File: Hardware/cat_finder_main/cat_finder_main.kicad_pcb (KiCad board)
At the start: 2 copper layers, 85 x 70 mm, 38 parts, among them J1 BATT, J10 Analog, J2 BME280, J3 CSS811, J4 DRIVERS, J5 GY-87, J7 FTDI, J8 Digital, U1 LD1117A33, U2 MCP732831CHARGER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

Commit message: clone other repo
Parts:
- renumbered SDA to J6, I2C to J9
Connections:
- J3 pad 5: /WAKE -> GND
- J3 pad 6: /INTCSS -> +3V3
- J3 pad 7: /RESET -> +3V3
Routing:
- net +3V3: track 170.8 -> 177.9 mm

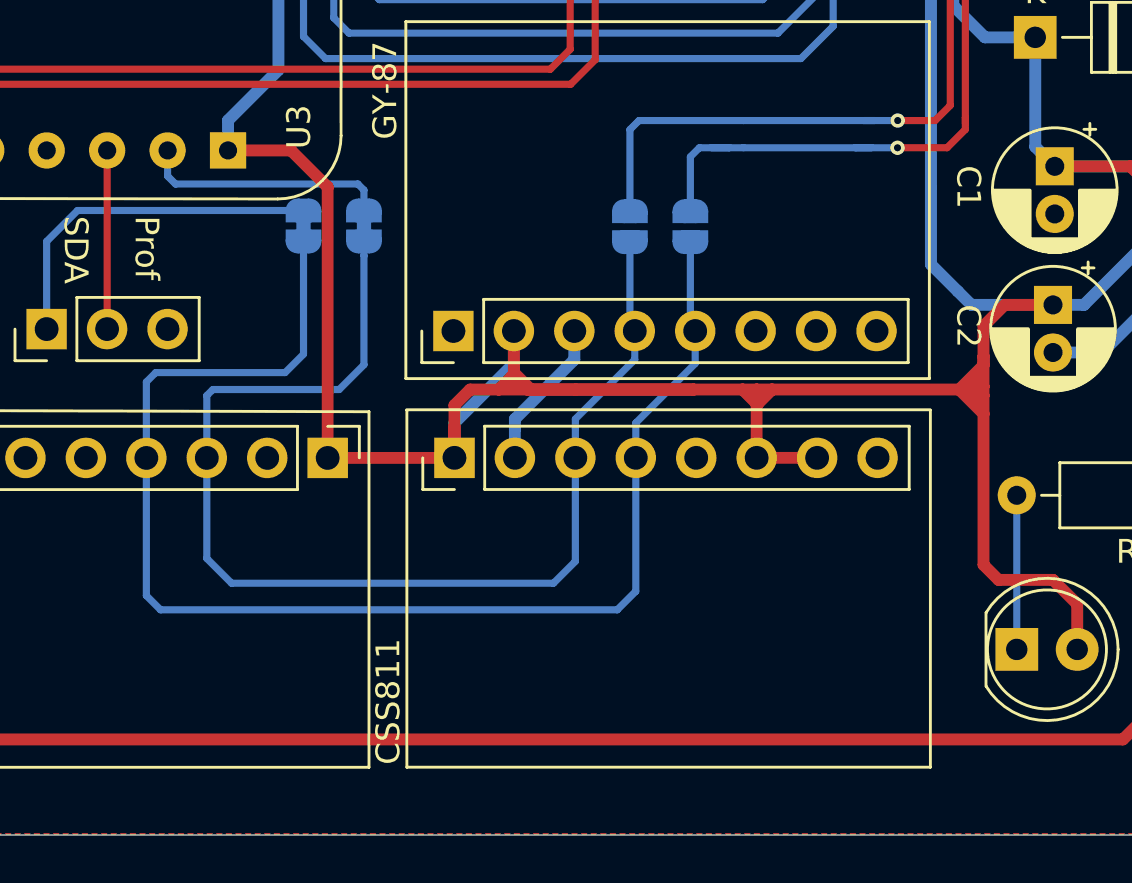
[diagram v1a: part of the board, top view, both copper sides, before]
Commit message: change CCS811
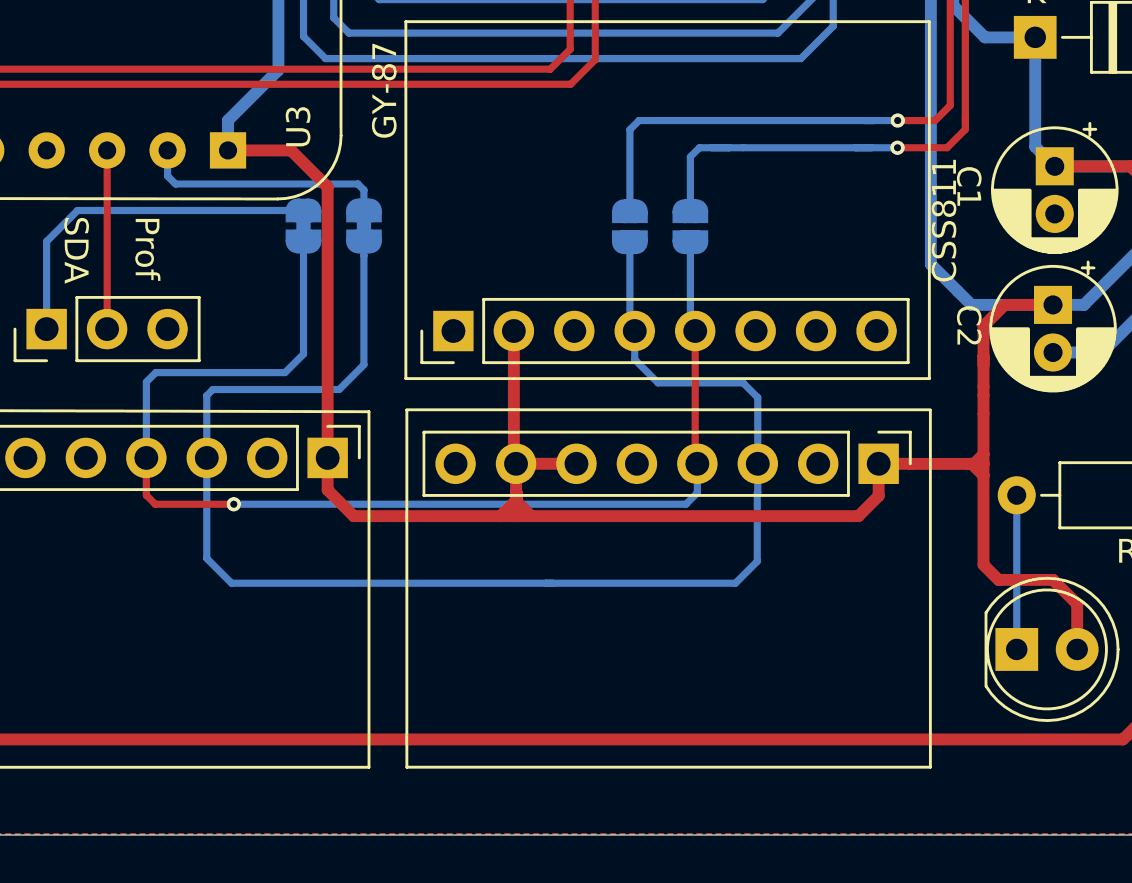
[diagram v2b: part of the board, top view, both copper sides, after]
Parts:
- moved J3 17.8 mm to (162.6, 114.5), turned to 270 degrees
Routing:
- net +3V3: track 177.9 -> 162.6 mm
- net /SCL: track 49.8 -> 60.9 mm
- net /SDA: track 57.5 -> 50.5 mm, vias 0 -> 1
- net GND: track 23.3 -> 16.9 mm

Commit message: labels battery
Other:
- board text added: "5V IN"
- board text added: "Battery Out"
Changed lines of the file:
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@@
   (general
     (thickness 1.6)
-    (drawings 6386)
+    (drawings 6388)
     (tracks 304)
     (zones 0)
@@
   (page A4)
   (layers
-    (0 F.Cu signal)
-    (31 B.Cu signal)
+    (0 F.Cu signal hide)
+    (31 B.Cu signal hide)
     (32 B.Adhes user)
     (33 F.Adhes user)
@@
     )
   )
+  (gr_text "Battery Out" (at 179.8 87 90) (layer F.SilkS)
+    (effects (font (size 1 1) (thickness 0.15)))
+  )
+  (gr_text "5V IN" (at 168.2 86.9 270) (layer F.SilkS)
+    (effects (font (size 1 1) (thickness 0.15)))
+  )
   (gr_line (start 119.38 119.38) (end 165.1 119.38) (layer B.SilkS) (width 0.12))

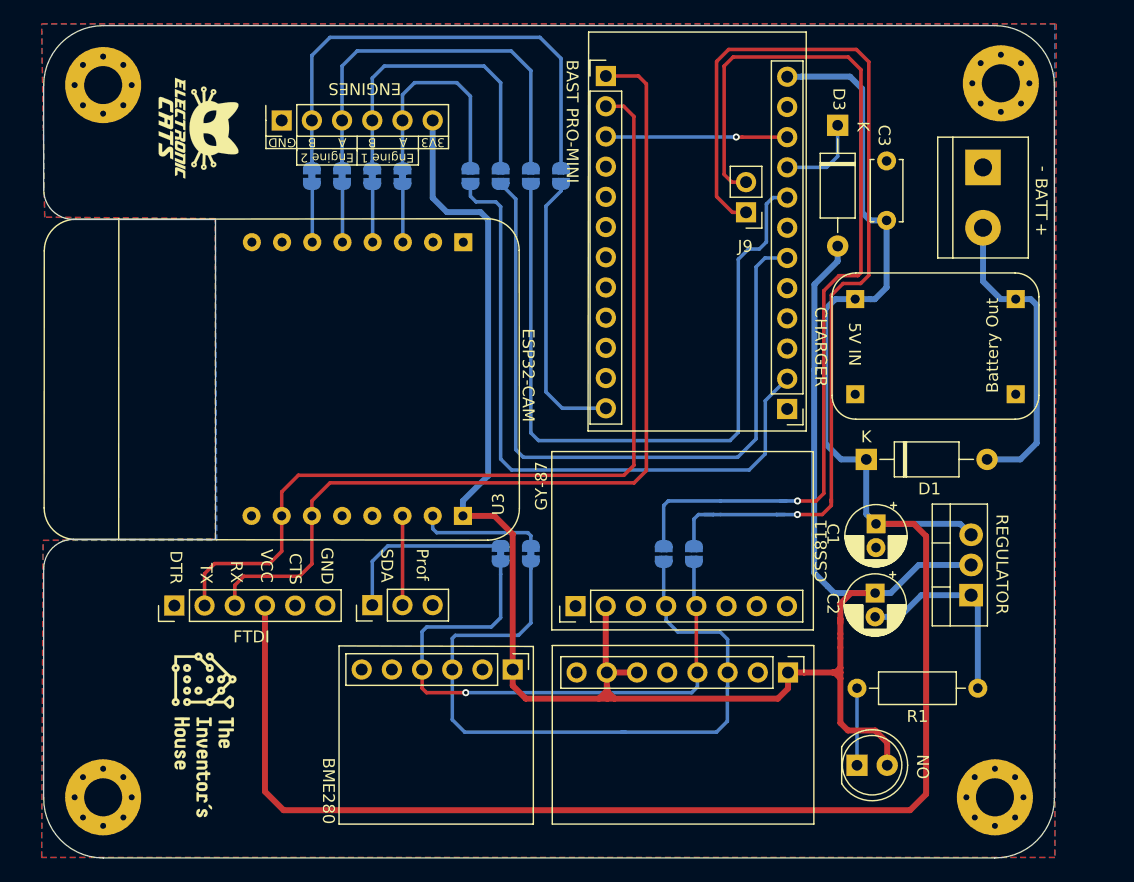
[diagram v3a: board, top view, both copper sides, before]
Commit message: change drill esp32
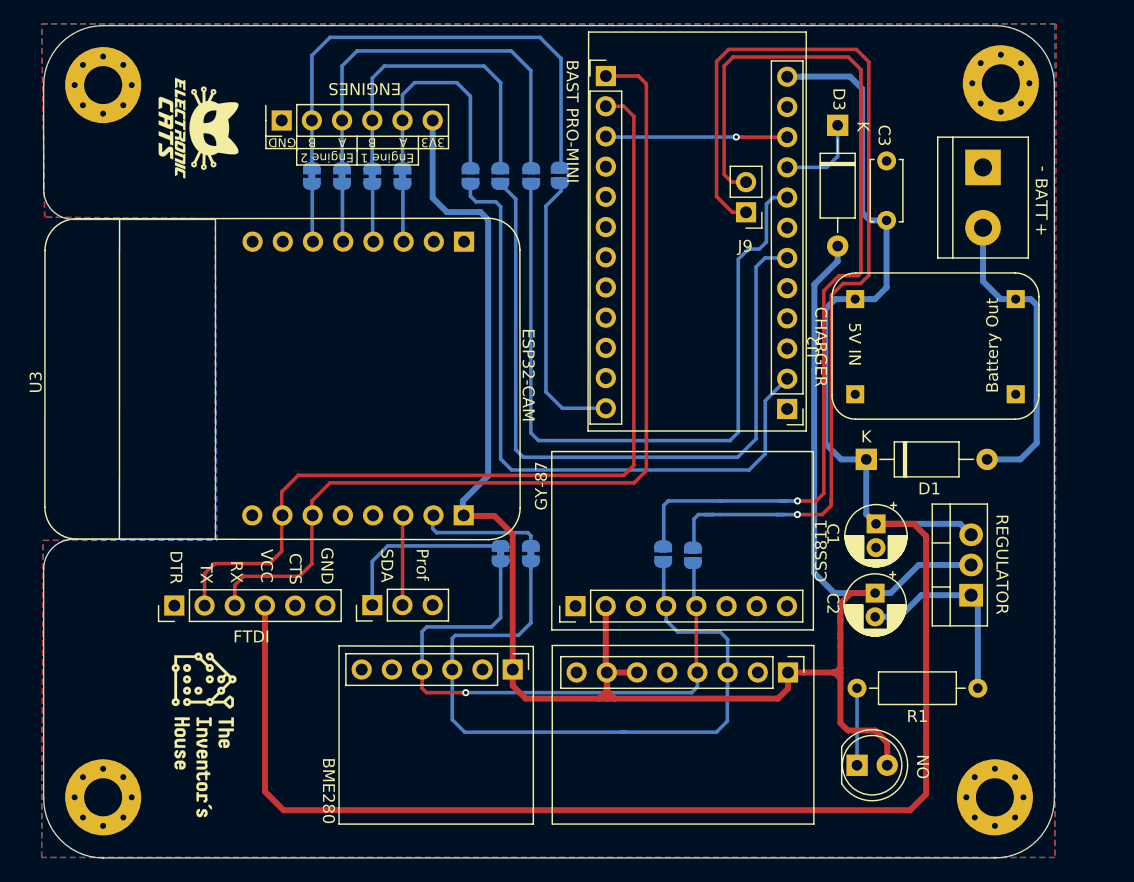
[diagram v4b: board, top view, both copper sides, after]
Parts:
- JP7: value Engine 1A -> Engine 1 A
- moved JP5 0.14 mm to (154.6, 104.7)
- moved JP10 0.12 mm to (143.4, 72.7)
- moved U3 0.07 mm to (124.8, 89.8)

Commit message: add switch
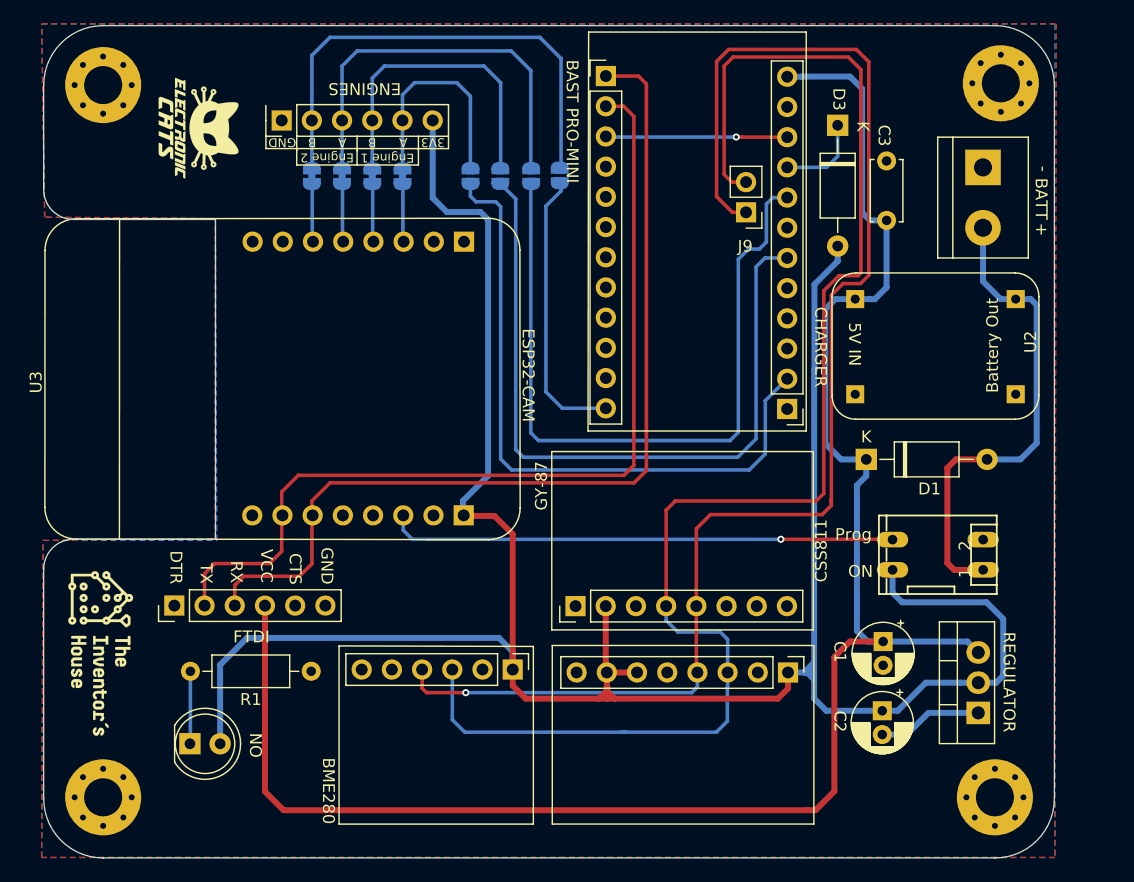
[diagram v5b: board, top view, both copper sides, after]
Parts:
- removed J6: Prog, Connector_PinHeader_2.54mm:PinHeader_1x03_P2.54mm_Vertical
- removed JP11: SDE ESP, Jumper:SolderJumper-2_P1.3mm_Bridged_RoundedPad1.0x1.5mm
- removed JP12: SCL ESP, Jumper:SolderJumper-2_P1.3mm_Bridged_RoundedPad1.0x1.5mm
- removed JP5: SDA, Jumper:SolderJumper-2_P1.3mm_Open_RoundedPad1.0x1.5mm
- removed JP6: SCL, Jumper:SolderJumper-2_P1.3mm_Open_RoundedPad1.0x1.5mm
- added SW1: SW_DIP_x02, connectors:DP-02, F.Cu at (175.2, 104.6)
- moved D2 56.1 mm to (112.3, 120.5)
- moved R1 56.1 mm to (122.5, 114.4)
- moved G*** 11.1 mm to (104.8, 112.9)
- moved C2 9.92 mm to (170.5, 117.7)
- moved C1 9.92 mm to (170.6, 111.9)
- moved U1 9.92 mm to (178.6, 117.9)
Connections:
- J9 pad 1: /SDAB -> /SDA
- J9 pad 2: /SCLB -> /SCL
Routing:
- net /SDAB: track 83.5 -> 0.00 mm, vias 1 -> 0
- net /SCLB: track 79.1 -> 0.00 mm, vias 1 -> 0
- net /SDA: track 50.5 -> 118.4 mm
- net /SCL: track 60.9 -> 125.7 mm
- net +3V3: track 162.6 -> 205.3 mm
- net /GPIO0: track 7.46 -> 42.7 mm, vias 0 -> 1
- net /SDAE: track 15.0 -> 0.00 mm
- net /BATT: track 26.2 -> 41.1 mm
- net /SCLE: track 10.4 -> 0.00 mm
- net GND: track 16.9 -> 9.62 mm
- net VCC: track 159.3 -> 152.8 mm
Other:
- board text added: "ON"
- board text added: "Prog"
- board text removed: "Prof"
- board text removed: "SDA"

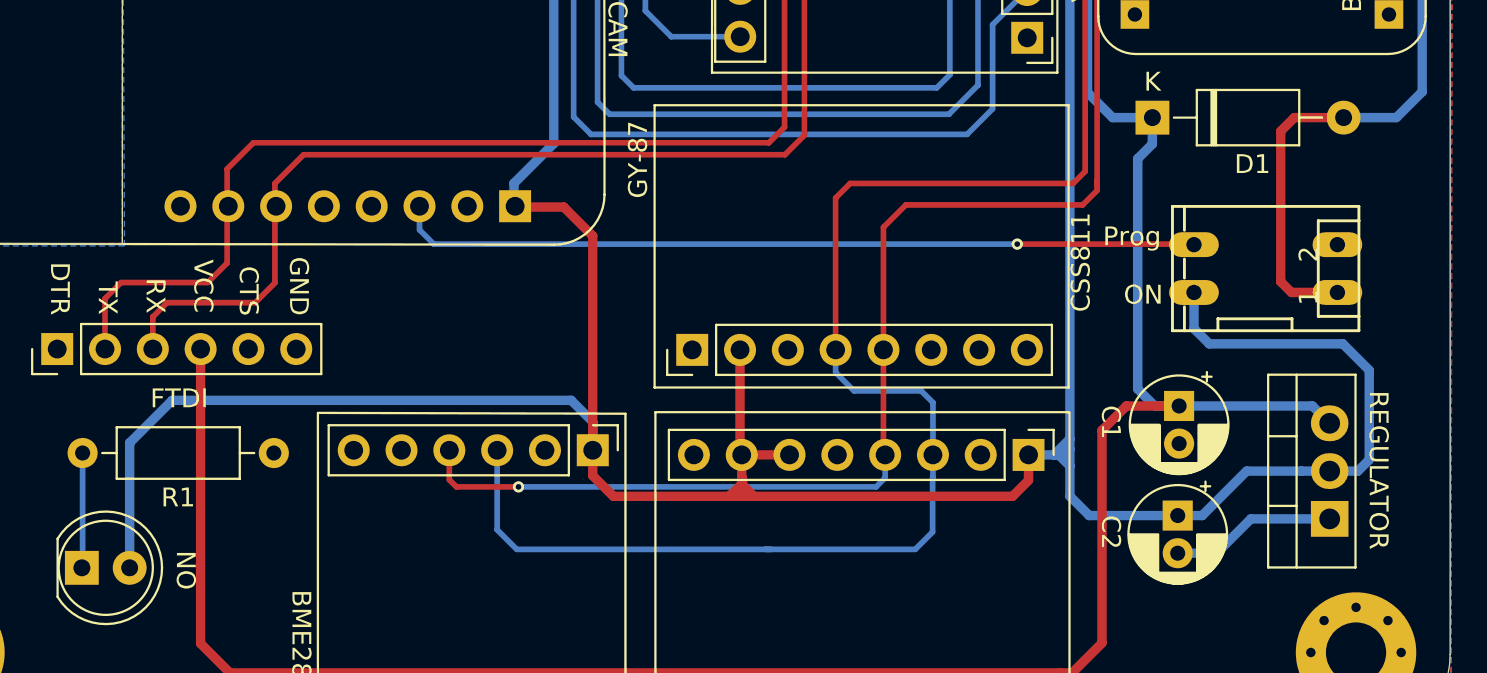
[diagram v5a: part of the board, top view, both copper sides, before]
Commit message: change prog pines delete switch
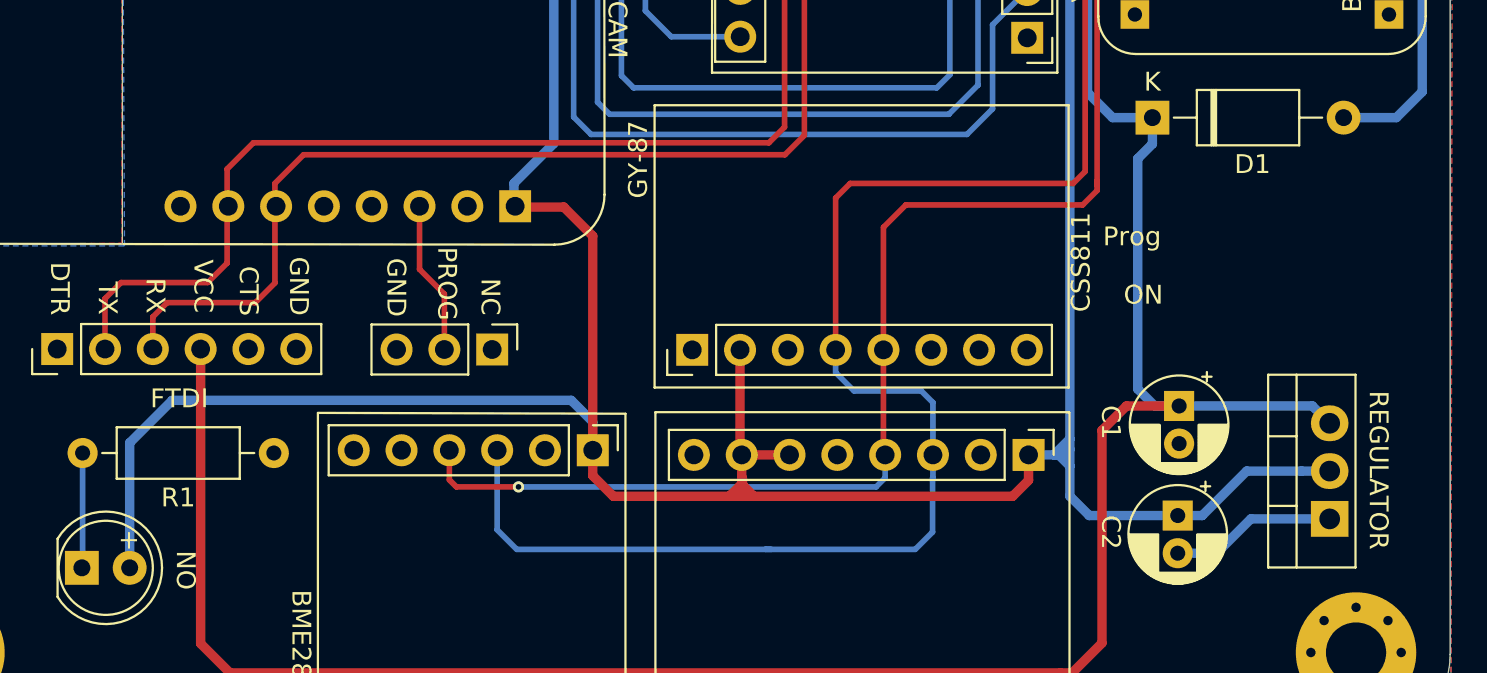
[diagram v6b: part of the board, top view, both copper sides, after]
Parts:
- removed SW1: SW_DIP_x02, connectors:DP-02
- added J6: PROG, Connector_PinHeader_2.54mm:PinHeader_1x03_P2.54mm_Vertical, F.Cu at (134.1, 108.9)
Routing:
- net /GPIO0: track 42.7 -> 8.16 mm, vias 1 -> 0
- net +3V3: track 205.3 -> 186.0 mm
- net /BATT: track 41.1 -> 26.2 mm
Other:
- board text added: "NC"
- board text added: "PROG"

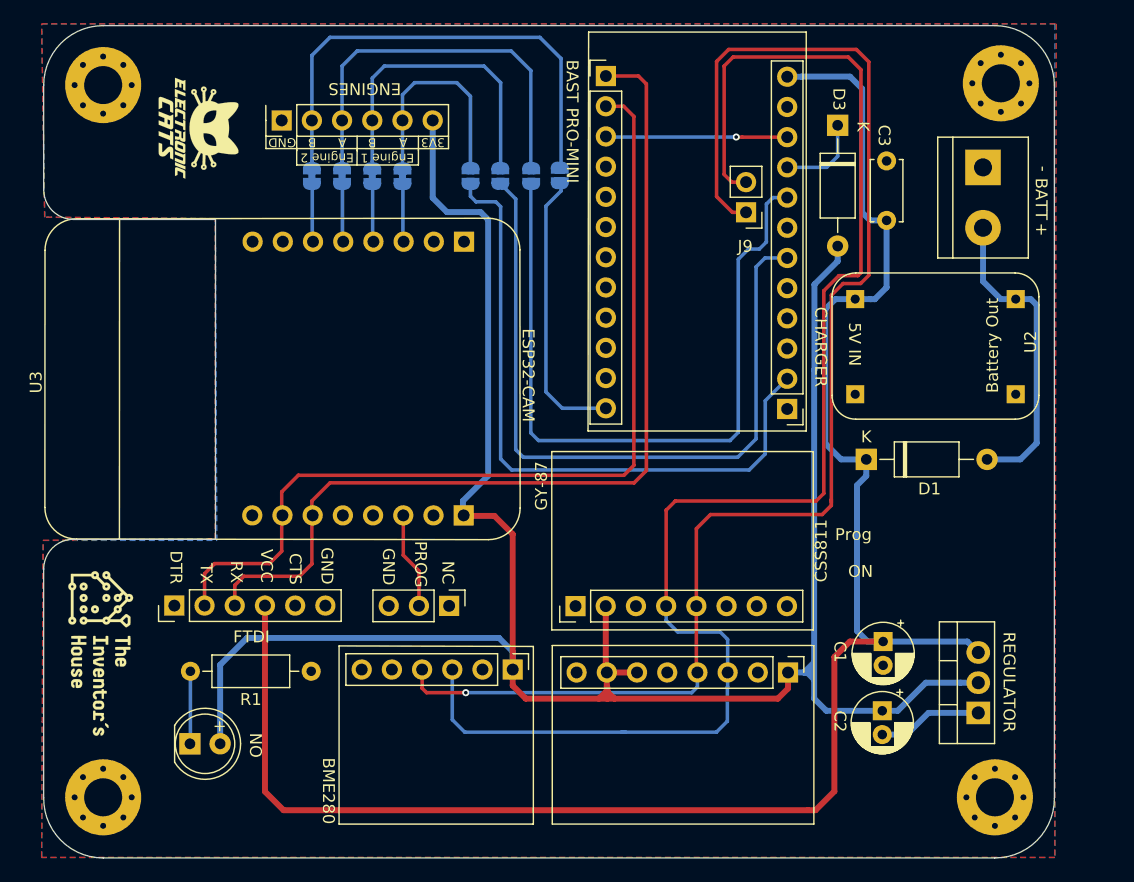
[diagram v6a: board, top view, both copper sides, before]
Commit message: add swich on/off
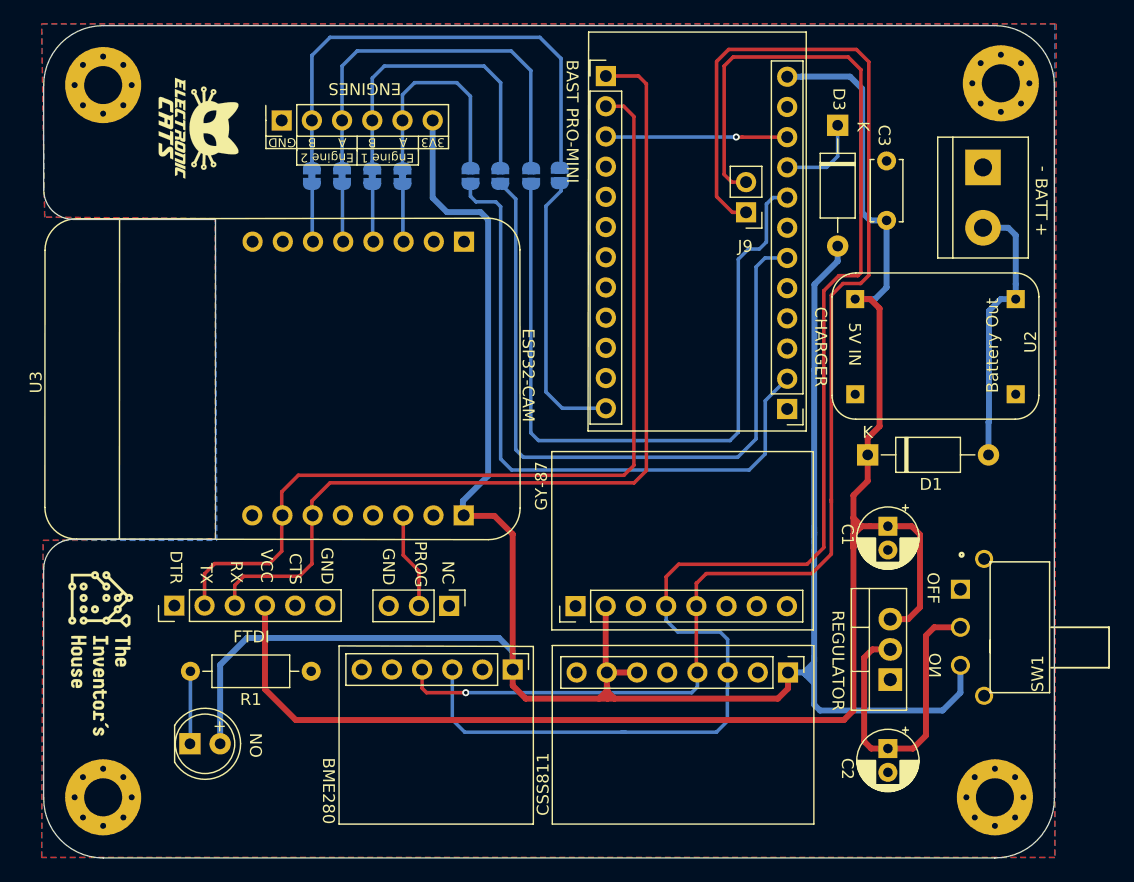
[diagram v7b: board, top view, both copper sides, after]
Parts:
- added SW1: ON Battery, connectors:SW_1825116-1, F.Cu at (177.1, 107.5)
- moved C1 9.71 mm to (171.0, 102.2)
- moved U1 7.91 mm to (171.2, 115.1)
- moved C2 3.21 mm to (171.0, 120.9)
- moved D1 0.40 mm to (169.3, 96.2)
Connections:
- C2 pad 1: +3V3 -> Net-(C2-Pad1)
- U1 pad 2: +3V3 -> Net-(C2-Pad1)
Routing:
- net Net-(C2-Pad1): track 0.00 -> 27.0 mm
- net VCC: track 152.8 -> 141.2 mm
- net GND: track 9.62 -> 0.00 mm
- net /BATT: track 26.2 -> 23.2 mm
- net +3V3: track 186.0 -> 188.1 mm
- net /SCL: track 125.7 -> 125.1 mm
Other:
- board text added: "OFF"
- board text removed: "Prog"
